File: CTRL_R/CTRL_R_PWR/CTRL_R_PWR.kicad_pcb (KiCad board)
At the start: 2 copper layers, 33.4 x 88 mm, 26 parts, among them J1 BM14B-NSHSS-TBT_LF__SN_, J2 BM04B-NSHSS-TBT_LF__SN_, J3 5051100592, U2 74LVC1G08

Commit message: Created CTRL_R_PWR Placeholder files
Also removed unnecessary "PWR_Button" Global Label in CTRL_R
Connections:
- J1 pad 6: unconnected-(J1-Pad6) -> PWR_BTN
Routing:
- net +3V3: track 39.0 -> 41.2 mm
- net GND: track 96.9 -> 96.2 mm
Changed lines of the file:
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@@
 		(sheetname "/")
 		(sheetfile "CTRL_R.kicad_sch")
-		(units
-			(unit
-				(name "A")
-				(pins "1" "2")
-			)
-		)
 		(attr smd)
 		(duplicate_pad_numbers_are_jumpers no)
@@
 		(sheetname "/")
 		(sheetfile "CTRL_R.kicad_sch")
-		(units
-			(unit
-				(name "A")
-				(pins "4" "2" "3" "1")
-			)
-		)
 		(attr smd)
 		(duplicate_pad_numbers_are_jumpers no)
@@
 		(sheetname "/")
 		(sheetfile "CTRL_R.kicad_sch")
-		(units
-			(unit
-				(name "A")
-				(pins)
-			)
-		)
 		(attr exclude_from_bom)
 		(duplicate_pad_numbers_are_jumpers no)
@@
 		(sheetname "/")
 		(sheetfile "CTRL_R.kicad_sch")
-		(units
-			(unit
-				(name "A")
-				(pins)
-			)
-		)
 		(attr exclude_from_bom)
 		(duplicate_pad_numbers_are_jumpers no)
@@
 		(sheetname "/")
 		(sheetfile "CTRL_R.kicad_sch")
-		(units
-			(unit
-				(name "A")
-				(pins "1" "2")
-			)
-		)
 		(attr smd)
 		(duplicate_pad_numbers_are_jumpers no)
@@
 		(sheetname "/")
 		(sheetfile "CTRL_R.kicad_sch")
-		(units
-			(unit
-				(name "A")
-				(pins "4" "2" "3" "1")
-			)
-		)
 		(attr smd)
 		(duplicate_pad_numbers_are_jumpers no)
@@
 		(sheetname "/")
 		(sheetfile "CTRL_R.kicad_sch")
-		(units
-			(unit
-				(name "A")
-				(pins)
-			)
-		)
 		(attr exclude_from_bom)
 		(duplicate_pad_numbers_are_jumpers no)
@@
 		(sheetname "/")
 		(sheetfile "CTRL_R.kicad_sch")
-		(units
-			(unit
-				(name "A")
-				(pins "1" "2")
-			)
-		)
 		(attr smd)
 		(duplicate_pad_numbers_are_jumpers no)
@@
 		(sheetname "/")
 		(sheetfile "CTRL_R.kicad_sch")
-		(units
-			(unit
-				(name "A")
-				(pins "4" "2" "3" "1")
-			)
-		)
 		(attr smd)
 		(duplicate_pad_numbers_are_jumpers no)
@@
 		(sheetname "/")
 		(sheetfile "CTRL_R.kicad_sch")
-		(units
-			(unit
-				(name "A")
-				(pins "4" "2" "3" "1")
-			)
-		)
 		(attr smd)
 		(duplicate_pad_numbers_are_jumpers no)
@@
 		(sheetname "/")
 		(sheetfile "CTRL_R.kicad_sch")
-		(units
-			(unit
-				(name "A")
-				(pins "4" "2" "3" "1")
-			)
-		)
 		(attr smd)
 		(duplicate_pad_numbers_are_jumpers no)
@@
 		(sheetname "/")
 		(sheetfile "CTRL_R.kicad_sch")
-		(units
-			(unit
-				(name "A")
-				(pins "4" "2" "3" "1")
-			)
-		)
 		(attr smd)
 		(duplicate_pad_numbers_are_jumpers no)
@@
 		(sheetname "/")
 		(sheetfile "CTRL_R.kicad_sch")
-		(units
-			(unit
-				(name "A")
-				(pins)
-			)
-		)
 		(attr exclude_from_bom)
 		(duplicate_pad_numbers_are_jumpers no)
@@
 		(sheetname "/")
 		(sheetfile "CTRL_R.kicad_sch")
-		(units
-			(unit
-				(name "A")
-				(pins)
-			)
-		)
 		(attr exclude_from_bom)
 		(duplicate_pad_numbers_are_jumpers no)
@@
 		(sheetname "/")
 		(sheetfile "CTRL_R.kicad_sch")
-		(units
-			(unit
-				(name "A")
-				(pins "1" "2")
-			)
-		)
 		(attr smd)
 		(duplicate_pad_numbers_are_jumpers no)
@@
 		(sheetname "/")
 		(sheetfile "CTRL_R.kicad_sch")
-		(units
-			(unit
-				(name "A")
-				(pins "1" "2")
-			)
-		)
 		(attr smd)
 		(duplicate_pad_numbers_are_jumpers no)
@@
 		(sheetname "/")
 		(sheetfile "CTRL_R.kicad_sch")
-		(units
-			(unit
-				(name "A")
-				(pins "1" "2")
-			)
-		)
 		(attr smd)
 		(duplicate_pad_numbers_are_jumpers no)
@@
 		(sheetname "/")
 		(sheetfile "CTRL_R.kicad_sch")
-		(units
-			(unit
-				(name "A")
-				(pins "1" "2")
-			)
-		)
 		(attr smd)
 		(duplicate_pad_numbers_are_jumpers no)
@@
 		(sheetname "/")
 		(sheetfile "CTRL_R.kicad_sch")
-		(units
-			(unit
-				(name "A")
-				(pins "1" "2")
-			)
-		)
 		(attr smd)
 		(duplicate_pad_numbers_are_jumpers no)
@@
 		(sheetname "/")
 		(sheetfile "CTRL_R.kicad_sch")
-		(units
-			(unit
-				(name "A")
-				(pins "16" "15" "14" "13" "12" "11" "10" "9" "8" "7" "6" "5" "4" "3"
-					"2" "1"
-				)
-			)
-		)
 		(attr smd dnp)
 		(duplicate_pad_numbers_are_jumpers no)
@@
 			(size 0.6 1.7)
 			(layers "B.Cu" "B.Mask" "B.Paste")
-			(net "unconnected-(J1-Pad6)")
+			(net "PWR_BTN")
 			(pinfunction "6_6")
-			(pintype "passive+no_connect")
+			(pintype "passive")
 		)
 		(pad "7" smd rect
@@
 		(sheetname "/")
 		(sheetfile "CTRL_R.kicad_sch")
-		(units
-			(unit
-				(name "A")
-				(pins "1" "2" "5" "3" "4")
-			)
-		)
 		(attr smd)
 		(duplicate_pad_numbers_are_jumpers no)
@@
 		(sheetname "/")
 		(sheetfile "CTRL_R.kicad_sch")
-		(units
-			(unit
-				(name "A")
-				(pins "1" "2")
-			)
-		)
 		(attr smd)
 		(duplicate_pad_numbers_are_jumpers no)
@@
 		(sheetname "/")
 		(sheetfile "CTRL_R.kicad_sch")
-		(units
-			(unit
-				(name "A")
-				(pins "6" "5" "4" "3" "2" "1")
-			)
-		)
 		(attr smd)
 		(duplicate_pad_numbers_are_jumpers no)
@@
 		(sheetname "/")
 		(sheetfile "CTRL_R.kicad_sch")
-		(units
-			(unit
-				(name "A")
-				(pins "1" "2" "3" "4" "5" "P1" "P2")
-			)
-		)
 		(attr smd)
 		(duplicate_pad_numbers_are_jumpers no)
@@
 	)
 	(segment
-		(start 97.523 99.6505)
-		(end 90.5025 99.6505)
+		(start 105.568528 96.007)
+		(end 106.729 97.167472)
 		(width 0.2)
 		(layer "F.Cu")
@@
 	)
 	(segment
-		(start 106.729 97.167472)
+		(start 87.869 96.007)
 		(end 105.568528 96.007)
 		(width 0.2)
@@
 	)
 	(segment
-		(start 84.116756 93.264756)
-		(end 86.859 96.007)
-		(width 0.2)
-		(layer "F.Cu")
-		(net "+3V3")
-	)
-	(segment
-		(start 106.729 97.751)
-		(end 106.729 97.167472)
+		(start 85.567 93.705)
+		(end 91.5125 99.6505)
 		(width 0.2)
 		(layer "F.Cu")
@@
 	)
 	(segment
-		(start 84.113962 93.264756)
-		(end 84.116756 93.264756)
+		(start 85.567 93.705)
+		(end 87.869 96.007)
 		(width 0.2)
 		(layer "F.Cu")
@@
 	)
 	(segment
-		(start 105.568528 96.007)
-		(end 86.859 96.007)
+		(start 106.729 97.167472)
+		(end 106.729 97.751)
 		(width 0.2)
 		(layer "F.Cu")
@@
 	)
 	(segment
-		(start 90.5025 99.6505)
-		(end 86.859 96.007)
+		(start 91.5125 99.6505)
+		(end 97.523 99.6505)
 		(width 0.2)
 		(layer "F.Cu")
@@
 	)
 	(via
-		(at 84.113962 93.264756)
+		(at 85.567 93.705)
 		(size 0.6)
 		(drill 0.3)
@@
 	)
 	(segment
+		(start 85.126756 93.264756)
+		(end 85.567 93.705)
+		(width 0.2)
+		(layer "B.Cu")
+		(net "+3V3")
+	)
+	(segment
 		(start 106.731001 97.753001)
 		(end 106.731001 99.761)
@@
 	)
 	(segment
+		(start 84.113962 93.264756)
+		(end 85.126756 93.264756)
+		(width 0.2)
+		(layer "B.Cu")
+		(net "+3V3")
+	)
+	(segment
 		(start 102.966 101.103)
 		(end 102.966 99.869001)
@@
 	)
 	(segment
-		(start 83.363962 97.264756)
-		(end 84.113962 97.264756)
+		(start 79.8 107)
+		(end 79.8 100.8)
 		(width 0.2)
 		(layer "B.Cu")
@@
 	)
 	(segment
-		(start 82.863962 94.264756)
-		(end 82.863962 96.764756)
-		(width 0.2)
-		(layer "B.Cu")
-		(net "GND")
-	)
-	(segment
-		(start 79.8 107)
-		(end 79.8 100.8)
+		(start 85.263962 94.664756)
+		(end 85.263962 96.864756)
 		(width 0.2)
 		(layer "B.Cu")
@@
 	)
 	(segment
-		(start 82.863962 96.764756)
-		(end 83.363962 97.264756)
+		(start 105.231001 99.761)
+		(end 105.231001 100.650999)
 		(width 0.2)
 		(layer "B.Cu")
@@
 	)
 	(segment
-		(start 105.231001 99.761)
-		(end 105.231001 100.650999)
+		(start 84.863962 94.264756)
+		(end 85.263962 94.664756)
 		(width 0.2)
 		(layer "B.Cu")
@@
 		(width 0.2)
 		(layer "B.Cu")
+		(net "GND")
+	)
+	(segment
+		(start 85.263962 96.864756)
+		(end 84.863962 97.264756)
+		(width 0.2)
+		(layer "B.Cu")

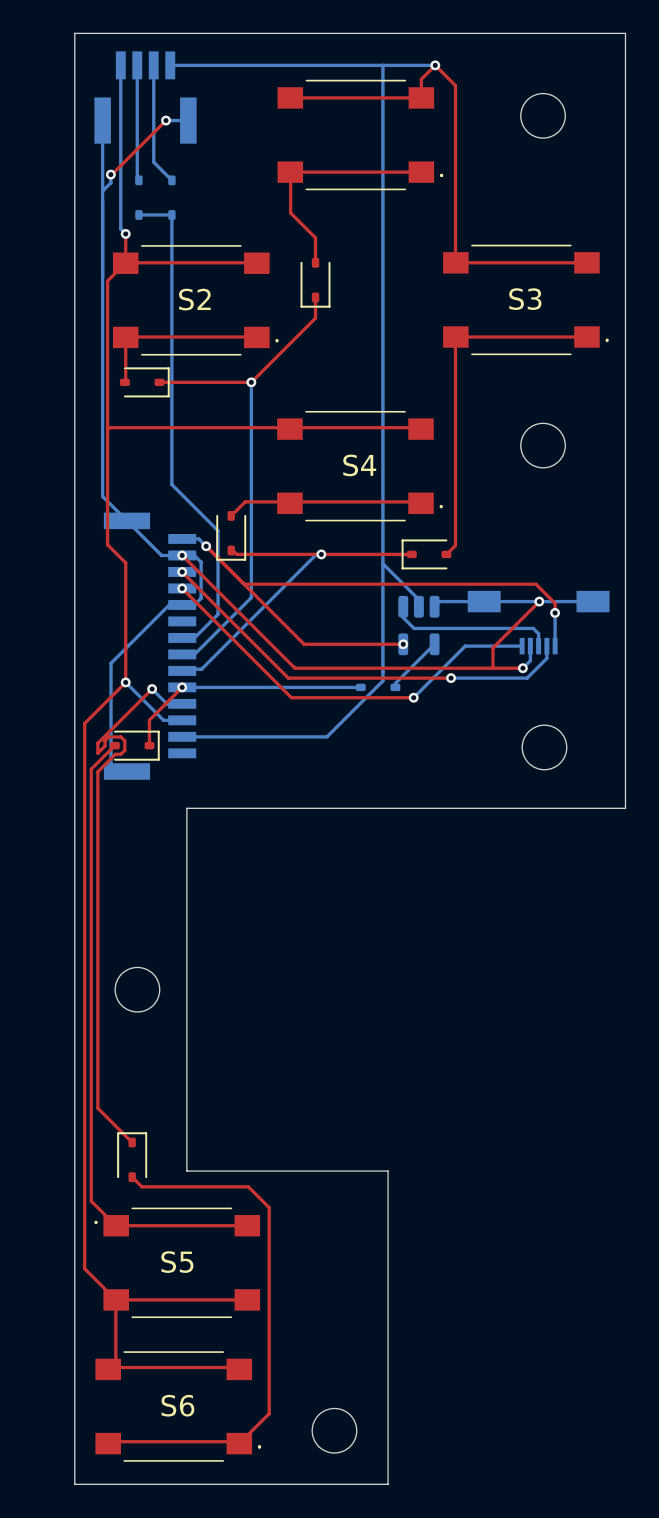
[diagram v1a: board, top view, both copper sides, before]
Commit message: CTRL_R_PWR Complete!
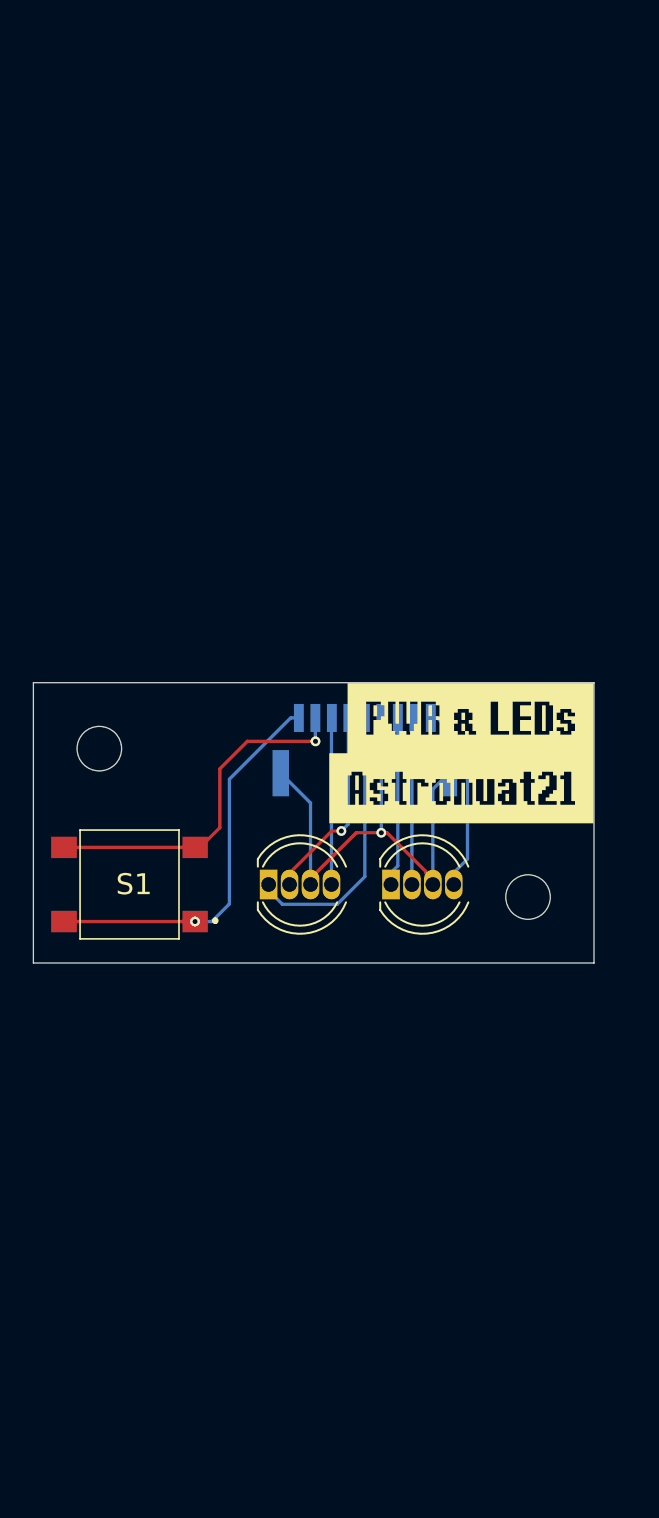
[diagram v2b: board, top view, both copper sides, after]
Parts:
- removed D3, D4, D5, D6, D7, D8, D9: 1N4148WS, Diode_SMD:D_SOD-323
- removed H3, H4, H5: MountingHole, MountingHole:MountingHole_2.7mm_M2.5
- removed J2: BM04B-NSHSS-TBT_LF__SN_, BM04B-NSHSS-TBT:BM04BNSHSSTBTLFSN
- removed J3: 5051100592, 5051100592:CON_5051100592_MOL
- removed S2, S3, S4, S5, S6: B3S-1000, B3S-1000:B3S1000
- removed U2: 74LVC1G08, Package_TO_SOT_SMD:SOT-23-5
- removed kibuzzard-6A187131: G***, kibuzzard-6A187131
- removed kibuzzard-6A19F3B7: G***, kibuzzard-6A19F3B7
- added kibuzzard-6A2CA9F9: G***, kibuzzard-6A2CA9F9, F.Cu at (101.6, 104.1)
- added kibuzzard-6A2CAA19: G***, kibuzzard-6A2CAA19, F.Cu at (101.0, 108.4)
- D1: value 1N4148WS -> LED_PWR; footprint Diode_SMD:D_SOD-323 -> LED_THT:LED_D5.0mm-4_RGB
- D2: value 1N4148WS -> LED_WIFI; footprint Diode_SMD:D_SOD-323 -> LED_THT:LED_D5.0mm-4_RGB
- J1: value BM14B-NSHSS-TBT_LF__SN_ -> BM09B-NSHSS-TBT_LF__SN_; footprint BM14B-NSHSS-TBT:BM14BNSHSSTBTLFSN -> BM09B-NSHSS-TBT_LF__SN_:BM09BNSHSSTBTLFSN
- S1: value B3S-1000 -> B3S-1002; footprint B3S-1000:B3S1000 -> B3S-1002:B3S1002
- moved S1 47.5 mm to (80.9, 114.2)
- moved H1 46.9 mm to (79.1, 106.0)
- moved D1 36.8 mm to (89.4, 114.2), turned to 0 degrees
- moved D2 34.0 mm to (96.8, 114.2), turned to 0 degrees
- moved H2 27.4 mm to (105.1, 115.0)
- moved J1 16.0 mm to (95.2, 108.6), turned to 180 degrees
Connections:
- D1 pad 1: Row2 -> Net-(D1-BA)
- D1 pad 2: Net-(D1-A) -> Net-(D1-GA)
- D2 pad 1: Row2 -> Net-(D2-BA)
- D2 pad 2: Net-(D2-A) -> Net-(D2-GA)
- J1 pad 1: +3V3 -> Net-(S1-COM_1)
- J1 pad 2: GND -> +3V3
- J1 pad 3: /ADC_X -> Net-(D1-RA)
- J1 pad 4: /ADC_Y -> Net-(D1-GA)
- J1 pad 5: GND -> Net-(D1-BA)
- J1 pad 6: PWR_BTN -> GND
- J1 pad 7: Row1 -> Net-(D2-BA)
- J1 pad 8: Row2 -> Net-(D2-GA)
- J1 pad 9: Row3 -> Net-(D2-RA)
- S1 pad 1: Net-(D1-A) -> Net-(S1-COM_1)
- S1 pad 2: Net-(D1-A) -> Net-(S1-COM_1)
- S1 pad 3: Col4 -> +3V3
- S1 pad 4: Col4 -> +3V3
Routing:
- net Col3: track 129.3 -> 0.00 mm, vias 2 -> 0
- net Col4: track 101.2 -> 0.00 mm, vias 1 -> 0
- net GND: track 96.2 -> 31.1 mm, vias 5 -> 1
- net Net-(D5-A): track 38.3 -> 0.00 mm
- net Row5: track 35.9 -> 0.00 mm, vias 1 -> 0
- net Net-(D6-A): track 32.1 -> 0.00 mm
- net Row2: track 30.3 -> 0.00 mm, vias 1 -> 0
- net Row1: track 29.4 -> 0.00 mm
- net /ADC_X: track 26.0 -> 0.00 mm, vias 2 -> 0
- net /ADC_Y: track 24.7 -> 0.00 mm, vias 2 -> 0
- net Net-(S1-COM_1): track 0.00 -> 23.8 mm, vias 0 -> 1
- net Row3: track 22.3 -> 0.00 mm, vias 1 -> 0
- net Net-(D3-A): track 21.4 -> 0.00 mm
- net +3V3: track 41.2 -> 21.4 mm, vias 3 -> 1
- net Net-(D1-BA): track 0.00 -> 16.9 mm
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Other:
- board size 33.4 x 88 mm -> 34 x 17 mm
